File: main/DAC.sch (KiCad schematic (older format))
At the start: 10 parts

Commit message: Remove old DAC files. Connect amplifier to audio out
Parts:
- removed J?: AudioJack3, symbol Connector:AudioJack3
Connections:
- net OUT_L: now reaches IC?.7 (VOUTL)
- net OUT_R: now reaches IC?.8 (VOUTR)
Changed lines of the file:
@@
 $Descr A4 11693 8268
 encoding utf-8
-Sheet 6 7
+Sheet 6 6
 Title ""
 Date ""
@@
 	1    0    0    -1
 $EndComp
-$Comp
-L Connector:AudioJack3 J?
-U 1 1 6149A5BA
-P 5000 5550
-F 0 "J?" H 4982 5875 50  0000 C CNN
-F 1 "AudioJack3" H 4982 5784 50  0000 C CNN
-F 2 "" H 5000 5550 50  0001 C CNN
-F 3 "~" H 5000 5550 50  0001 C CNN
-	1    5000 5550
-	0    -1   -1   0
-$EndComp
 Wire Wire Line
 	5050 4350 5000 4350
-$Comp
-L power:GNDA #PWR?
-U 1 1 6149B0F4
-P 5100 5350
-F 0 "#PWR?" H 5100 5100 50  0001 C CNN
-F 1 "GNDA" H 5105 5177 50  0000 C CNN
-F 2 "" H 5100 5350 50  0001 C CNN
-F 3 "" H 5100 5350 50  0001 C CNN
-	1    5100 5350
-	0    -1   -1   0
-$EndComp
 $Comp
 L Device:R R?
@@
 Wire Bus Line
 	2500 2550 3550 2550
+Text HLabel 4900 5350 3    50   Output ~ 0
+OUT_L
+Text HLabel 5000 5350 3    50   Output ~ 0
+OUT_R
 $EndSCHEMATC

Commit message: Set up switching regulator circuits.
We only use half of the switching regulator that generates the 1V0
voltage. I'm not sure if the half not being used is connected correctly.
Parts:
- IC1: renamed from IC?; footprint SOP63P600X175-16N -> DAC:SOP63P600X175-16N
- gave numbers to parts that had none: 8
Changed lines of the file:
@@
 $Descr A4 11693 8268
 encoding utf-8
-Sheet 6 6
+Sheet 5 7
 Title ""
 Date ""
@@
 $EndDescr
 $Comp
-L PCM1741E:PCM1741E IC?
+L PCM1741E:PCM1741E IC1
 U 1 1 614975F8
 P 5050 3650
-F 0 "IC?" H 5800 3915 50  0000 C CNN
+F 0 "IC1" H 5800 3915 50  0000 C CNN
 F 1 "PCM1741E" H 5800 3824 50  0000 C CNN
-F 2 "SOP63P600X175-16N" H 6400 3750 50  0001 L CNN
+F 2 "DAC:SOP63P600X175-16N" H 6400 3750 50  0001 L CNN
 F 3 "http://www.ti.com/lit/gpn/PCM1741" H 6400 3650 50  0001 L CNN
 F 4 "PCM1741E, Audio DAC Dual 24 bit-, 96ksps +/-6%FSR Serial (SPI), 16-Pin SSOP" H 6400 3550 50  0001 L CNN "Description"
@@
 AR Path="/6149F240" Ref="R?"  Part="1"
 AR Path="/61417224/6149F240" Ref="R?"  Part="1"
-AR Path="/61496F7B/6149F240" Ref="R?"  Part="1"
-F 0 "R?" V 3350 3300 50  0000 C CNN
+AR Path="/61496F7B/6149F240" Ref="R15"  Part="1"
+F 0 "R15" V 3350 3300 50  0000 C CNN
 F 1 "22-100" V 3250 3300 50  0000 C CNN
 F 2 "" V 3280 3300 50  0001 C CNN
@@
 AR Path="/6149F246" Ref="R?"  Part="1"
 AR Path="/61417224/6149F246" Ref="R?"  Part="1"
-AR Path="/61496F7B/6149F246" Ref="R?"  Part="1"
-F 0 "R?" V 3050 3300 50  0000 C CNN
+AR Path="/61496F7B/6149F246" Ref="R14"  Part="1"
+F 0 "R14" V 3050 3300 50  0000 C CNN
 F 1 "22-100" V 2950 3300 50  0000 C CNN
 F 2 "" V 2980 3300 50  0001 C CNN
@@
 AR Path="/6149F24C" Ref="R?"  Part="1"
 AR Path="/61417224/6149F24C" Ref="R?"  Part="1"
-AR Path="/61496F7B/6149F24C" Ref="R?"  Part="1"
-F 0 "R?" V 3650 3300 50  0000 C CNN
+AR Path="/61496F7B/6149F24C" Ref="R16"  Part="1"
+F 0 "R16" V 3650 3300 50  0000 C CNN
 F 1 "22-100" V 3550 3300 50  0000 C CNN
 F 2 "" V 3580 3300 50  0001 C CNN
@@
 AR Path="/614A0D57" Ref="R?"  Part="1"
 AR Path="/61417224/614A0D57" Ref="R?"  Part="1"
-AR Path="/61496F7B/614A0D57" Ref="R?"  Part="1"
-F 0 "R?" V 6650 2750 50  0000 C CNN
+AR Path="/61496F7B/614A0D57" Ref="R17"  Part="1"
+F 0 "R17" V 6650 2750 50  0000 C CNN
 F 1 "22-100" V 6550 2750 50  0000 C CNN
 F 2 "" V 6580 2750 50  0001 C CNN
@@
 NoConn ~ 6550 4150
 $Comp
-L Device:CP1 C?
+L Device:CP1 C42
 U 1 1 614A3178
 P 7250 4400
-F 0 "C?" H 7365 4446 50  0000 L CNN
+F 0 "C42" H 7365 4446 50  0000 L CNN
 F 1 "10uF" H 7365 4355 50  0000 L CNN
 F 2 "" H 7250 4400 50  0001 C CNN
@@
 	6550 4250 7250 4250
 $Comp
-L power:GNDA #PWR?
+L power:GNDA #PWR0149
 U 1 1 614A4529
 P 7250 4600
-F 0 "#PWR?" H 7250 4350 50  0001 C CNN
+F 0 "#PWR0149" H 7250 4350 50  0001 C CNN
 F 1 "GNDA" H 7255 4427 50  0000 C CNN
 F 2 "" H 7250 4600 50  0001 C CNN
@@
 	4700 4450 4700 4150
 $Comp
-L Device:CP1 C?
+L Device:CP1 C41
 U 1 1 614B25E2
 P 3750 4750
-F 0 "C?" H 3865 4796 50  0000 L CNN
+F 0 "C41" H 3865 4796 50  0000 L CNN
 F 1 "10uF" H 3865 4705 50  0000 L CNN
 F 2 "" H 3750 4750 50  0001 C CNN
@@
 $EndComp
 $Comp
-L power:GNDA #PWR?
+L power:GNDA #PWR0150
 U 1 1 614B2E1B
 P 3750 4900
-F 0 "#PWR?" H 3750 4650 50  0001 C CNN
+F 0 "#PWR0150" H 3750 4650 50  0001 C CNN
 F 1 "GNDA" H 3755 4727 50  0000 C CNN
 F 2 "" H 3750 4900 50  0001 C CNN
@@
 	3750 4450 4700 4450
 $Comp
-L power:+3.3VA #PWR?
+L power:+3.3VA #PWR0151
 U 1 1 614B4892
 P 2100 4900
-F 0 "#PWR?" H 2100 4750 50  0001 C CNN
+F 0 "#PWR0151" H 2100 4750 50  0001 C CNN
 F 1 "+3.3VA" H 2115 5073 50  0000 C CNN
 F 2 "" H 2100 4900 50  0001 C CNN
@@
 $EndComp
 $Comp
-L power:GND #PWR?
+L power:GND #PWR0152
 U 1 1 614B5261
 P 2150 3950
-F 0 "#PWR?" H 2150 3700 50  0001 C CNN
+F 0 "#PWR0152" H 2150 3700 50  0001 C CNN
 F 1 "GND" V 2155 3822 50  0000 R CNN
 F 2 "" H 2150 3950 50  0001 C CNN
@@
 	4600 4250 3750 4250
 $Comp
-L Device:CP1 C?
+L Device:CP1 C40
 U 1 1 614B8248
 P 3750 4100
-F 0 "C?" H 3865 4146 50  0000 L CNN
+F 0 "C40" H 3865 4146 50  0000 L CNN
 F 1 "10uF" H 3865 4055 50  0000 L CNN
 F 2 "" H 3750 4100 50  0001 C CNN
@@
 	4900 4250 5050 4250
 $Comp
-L Regulator_Linear:LM1084-3.3 U?
+L Regulator_Linear:LM1084-3.3 U5
 U 1 1 614C1BF7
 P 2700 4250
-F 0 "U?" H 2700 4492 50  0000 C CNN
+F 0 "U5" H 2700 4492 50  0000 C CNN
 F 1 "LM1084-3.3" H 2700 4401 50  0000 C CNN
 F 2 "" H 2700 4500 50  0001 C CIN
@@
 Connection ~ 3750 4450
 $Comp
-L power:GNDA #PWR?
+L power:GNDA #PWR0153
 U 1 1 614C8204
 P 2700 4550
-F 0 "#PWR?" H 2700 4300 50  0001 C CNN
+F 0 "#PWR0153" H 2700 4300 50  0001 C CNN
 F 1 "GNDA" H 2705 4377 50  0000 C CNN
 F 2 "" H 2700 4550 50  0001 C CNN
@@
 Text Label 6650 3950 0    50   ~ 0
 DAC_MODE_DATA
-Wire Bus Line
-	2500 2550 3550 2550
 Text HLabel 4900 5350 3    50   Output ~ 0
 OUT_L
 Text HLabel 5000 5350 3    50   Output ~ 0
 OUT_R
+Wire Bus Line
+	2500 2550 3550 2550
 $EndSCHEMATC

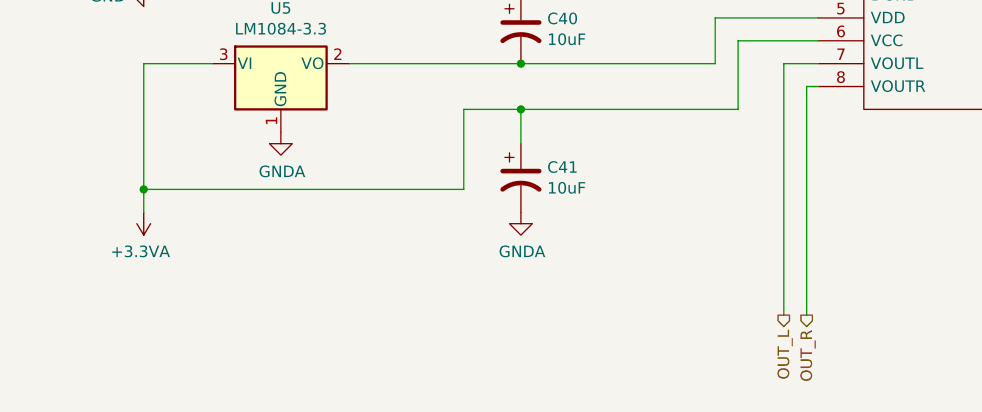
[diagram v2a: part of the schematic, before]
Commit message: Remove old EFM32GG lib
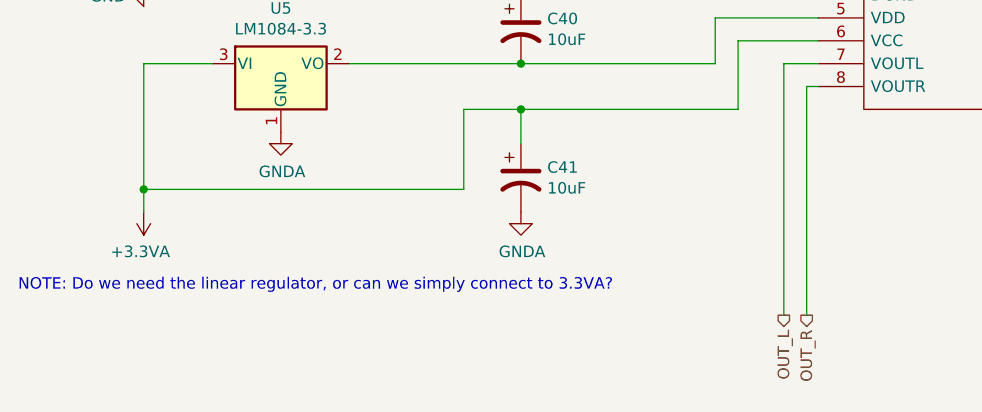
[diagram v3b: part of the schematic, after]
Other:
- note added: "NOTE: Do we need the linear regulator, or can we simply connect to 3.3VA?"
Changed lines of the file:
@@
 Wire Bus Line
 	2500 2550 3550 2550
+Text Notes 1550 5250 0    50   ~ 0
+NOTE: Do we need the linear regulator, or can we simply connect to 3.3VA?
 $EndSCHEMATC

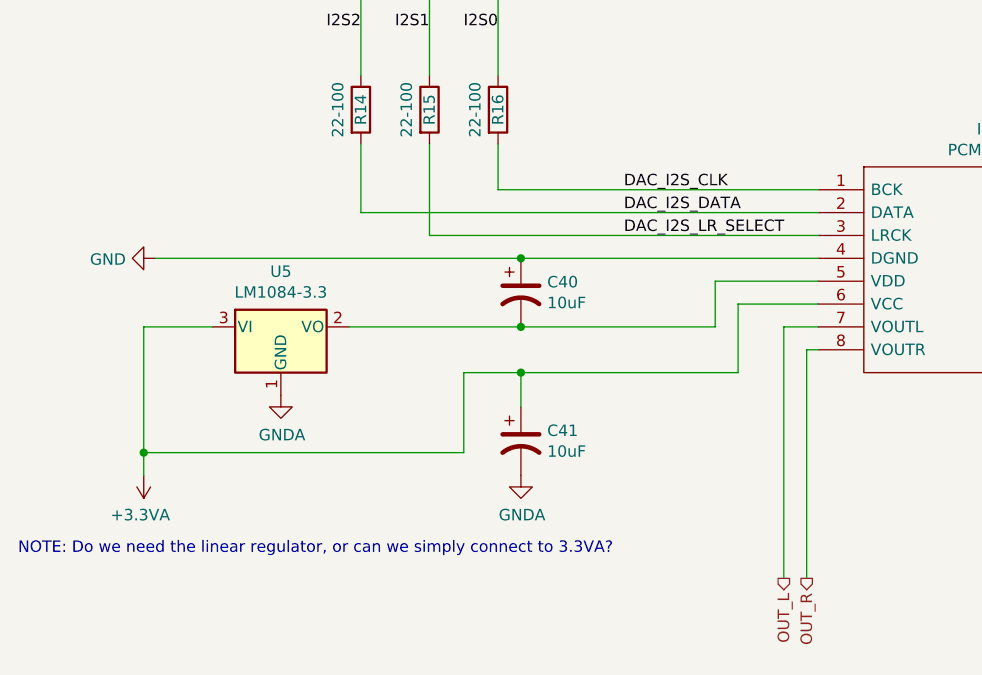
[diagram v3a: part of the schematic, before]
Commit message: Continue wiring of the MCU
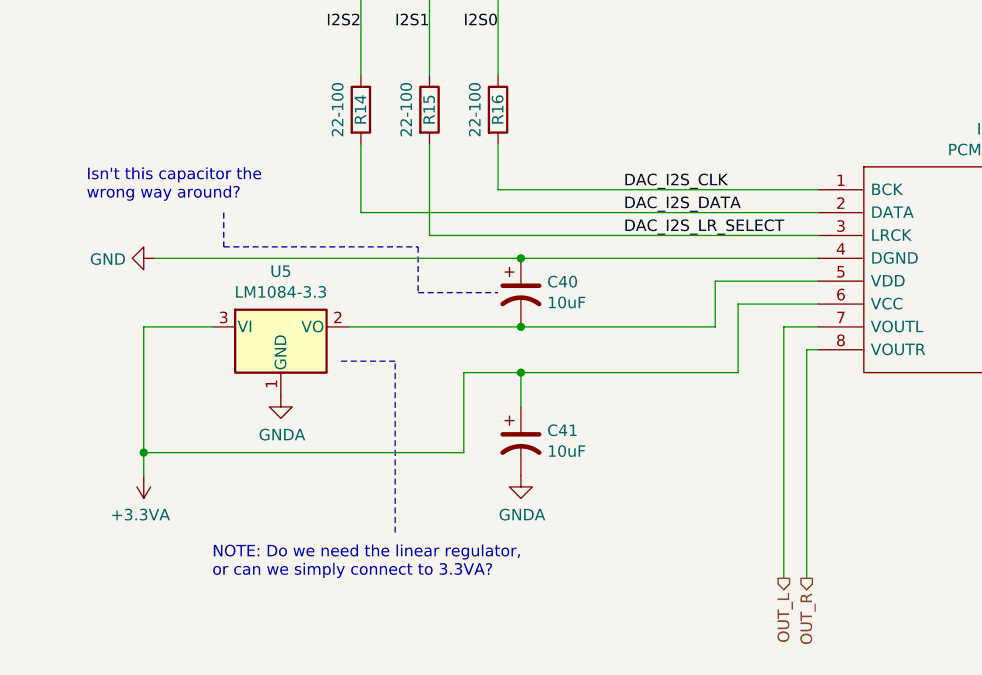
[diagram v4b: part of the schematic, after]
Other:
- note added: "Isn't this capacitor the\nwrong way around?"
- note added: "NOTE: Do we need the linear regulator,\nor can we simply connect to 3.3VA?"
- note removed: "NOTE: Do we need the linear regulator, or can we simply connect to 3.3VA?"
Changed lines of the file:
@@
 $Descr A4 11693 8268
 encoding utf-8
-Sheet 5 7
+Sheet 4 7
 Title ""
 Date ""
@@
 Text HLabel 5000 5350 3    50   Output ~ 0
 OUT_R
+Text Notes 2400 5350 0    50   ~ 0
+NOTE: Do we need the linear regulator,\nor can we simply connect to 3.3VA?
+Text Notes 1850 3700 0    50   ~ 0
+Isn't this capacitor the\nwrong way around?
+Wire Notes Line
+	2450 3750 2450 3900
+Wire Notes Line
+	2450 3900 3300 3900
+Wire Notes Line
+	3300 3900 3300 4100
+Wire Notes Line
+	3300 4100 3650 4100
+Wire Notes Line
+	3200 5150 3200 4400
+Wire Notes Line
+	3200 4400 2950 4400
 Wire Bus Line
 	2500 2550 3550 2550
-Text Notes 1550 5250 0    50   ~ 0
-NOTE: Do we need the linear regulator, or can we simply connect to 3.3VA?
 $EndSCHEMATC

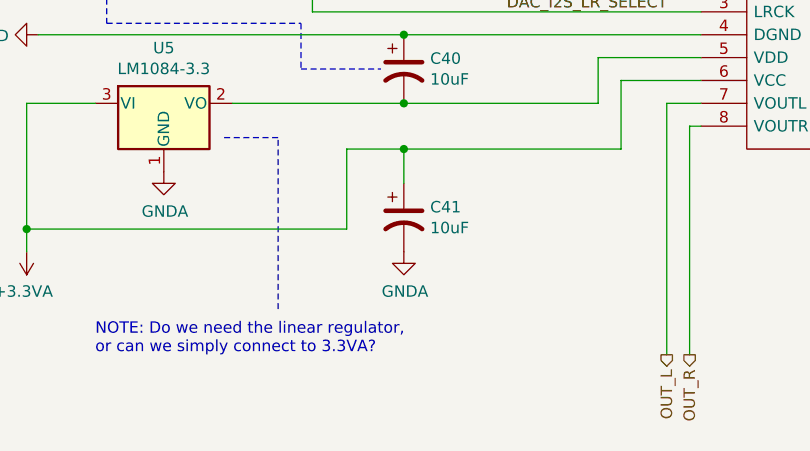
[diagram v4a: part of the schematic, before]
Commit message: Be consistent with capacitor values (always use F)
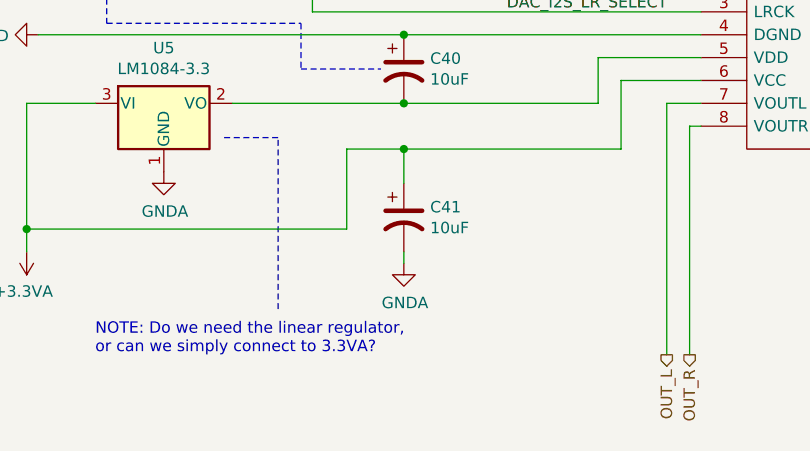
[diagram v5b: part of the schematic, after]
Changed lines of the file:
@@
-	1    0    0    -1
-$EndComp
-$Comp
-L power:GNDA #PWR0150
-U 1 1 614B2E1B
-P 3750 4900
-F 0 "#PWR0150" H 3750 4650 50  0001 C CNN
-F 1 "GNDA" H 3755 4727 50  0000 C CNN
-F 2 "" H 3750 4900 50  0001 C CNN
-F 3 "" H 3750 4900 50  0001 C CNN
-	1    3750 4900
 	1    0    0    -1
 $EndComp
@@
 Wire Notes Line
 	3200 4400 2950 4400
+Wire Wire Line
+	3750 4950 3750 4900
 Wire Bus Line
 	2500 2550 3550 2550
+$Comp
+L power:GNDA #PWR0150
+U 1 1 614C9464
+P 3750 4950
+F 0 "#PWR0150" H 3750 4700 50  0001 C CNN
+F 1 "GNDA" H 3755 4777 50  0000 C CNN
+F 2 "" H 3750 4950 50  0001 C CNN
+F 3 "" H 3750 4950 50  0001 C CNN
+	1    3750 4950
+	1    0    0    -1
+$EndComp
 $EndSCHEMATC

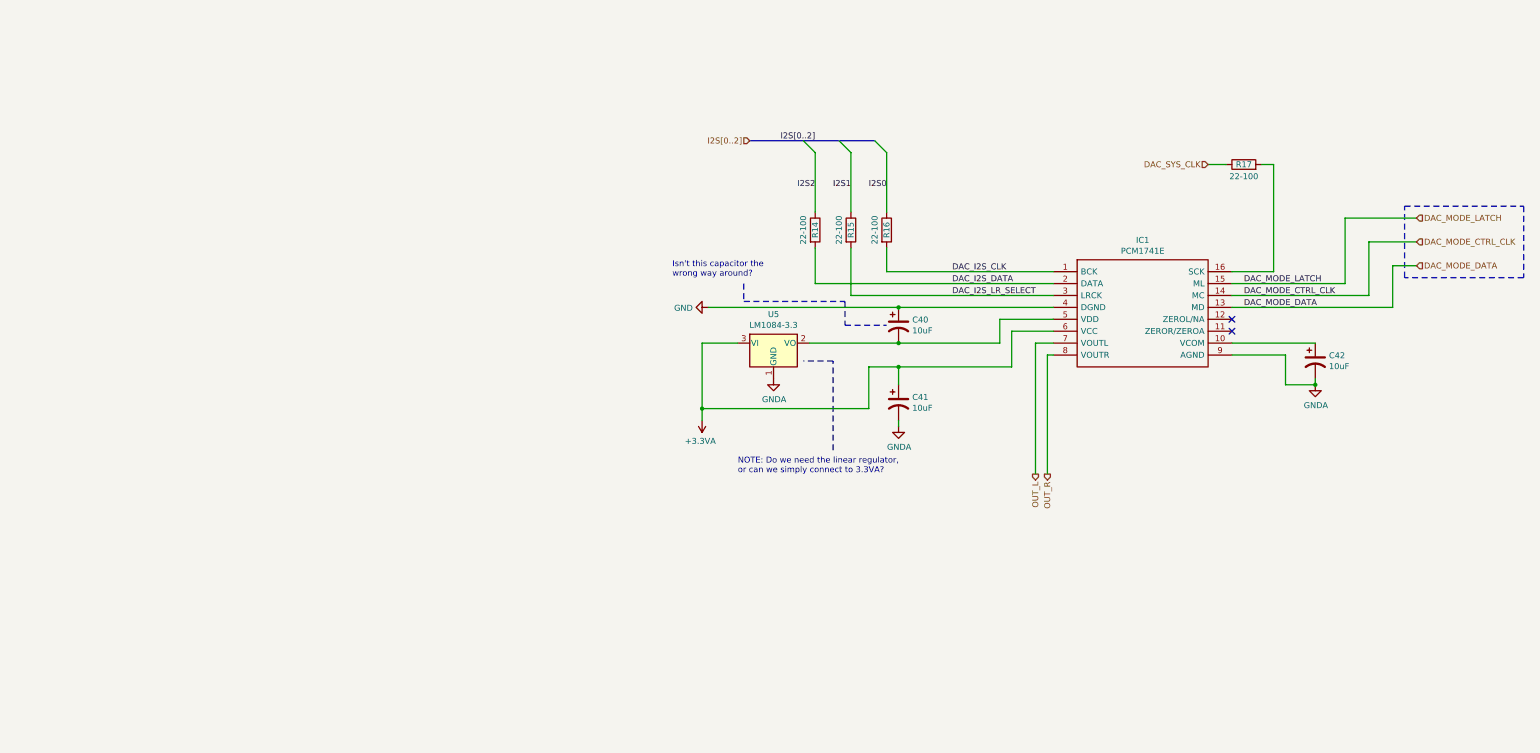
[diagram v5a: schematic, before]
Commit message: FPGA connections, DAC linear regulator removed, DAC I2S breakout
Connected the SPI, I2S and GPIO to some (mostly) arbitrary pins. Notably
the SPI clock has to be connected to a clock pin on the FPGA.

The linear regulator is (hopefully) not needed for the DAC as we already
have a separate analog +3.3V created by the switching regulators.

The I2S wires to the DAC are now connected to the FPGA as well as
breakout pins over 0 ohm resistors, in case we need to connect to an
external FPGA.
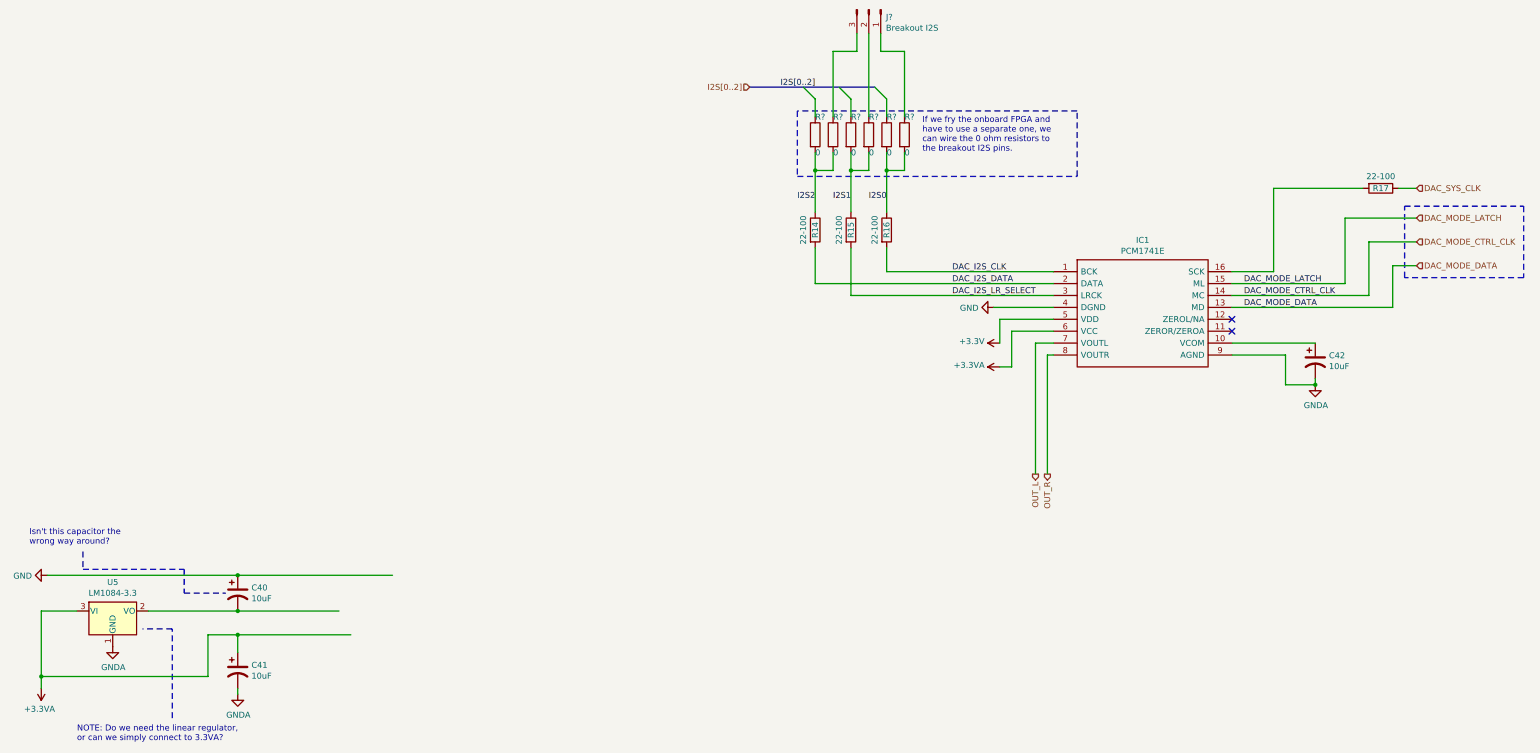
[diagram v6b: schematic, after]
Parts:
- added J?: Breakout I2S, symbol Connector:Conn_01x03_Male
- added R? (x6): 0, symbol Device:R
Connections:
- net labels added: +3.3V
- wire segments 48 -> 69
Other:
- note added: "If we fry the onboard FPGA and \nhave to use a separate one, we \ncan wire the 0 ohm resistors to \nthe breakout I2S pins."
- moved on the sheet: C40, C41, R17, U5

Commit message: Add FPGA RAM chip
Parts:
- removed C41: 10uF, symbol Device:CP1
- removed U5: LM1084-3.3, symbol Regulator_Linear:LM1084-3.3
- gave numbers to parts that had none: 7
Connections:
- net labels added: DAC_ZERO_L, DAC_ZERO_R
- wire segments 69 -> 61
- no-connect marks 2 -> 0
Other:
- note removed: "Isn't this capacitor the\nwrong way around?"
- note removed: "NOTE: Do we need the linear regulator,\nor can we simply connect to 3.3VA?"
- moved on the sheet: J12, R37, R39, R41
